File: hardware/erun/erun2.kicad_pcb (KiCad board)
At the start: 2 copper layers, 73.4 x 92.1 mm, 34 parts, among them J1 Conn_Coaxial, J10 Conn_01x03_Female, J2 HEIDENHAIN_MT25_TTL, J3 TRIGGER_TTL, J4 Conn_01x02_Female, J5 Conn_01x02_Female, J6 Conn_01x02_Female, J7 Conn_01x02_Female, J8 Conn_01x02_Female, J9 Conn_01x03_Female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

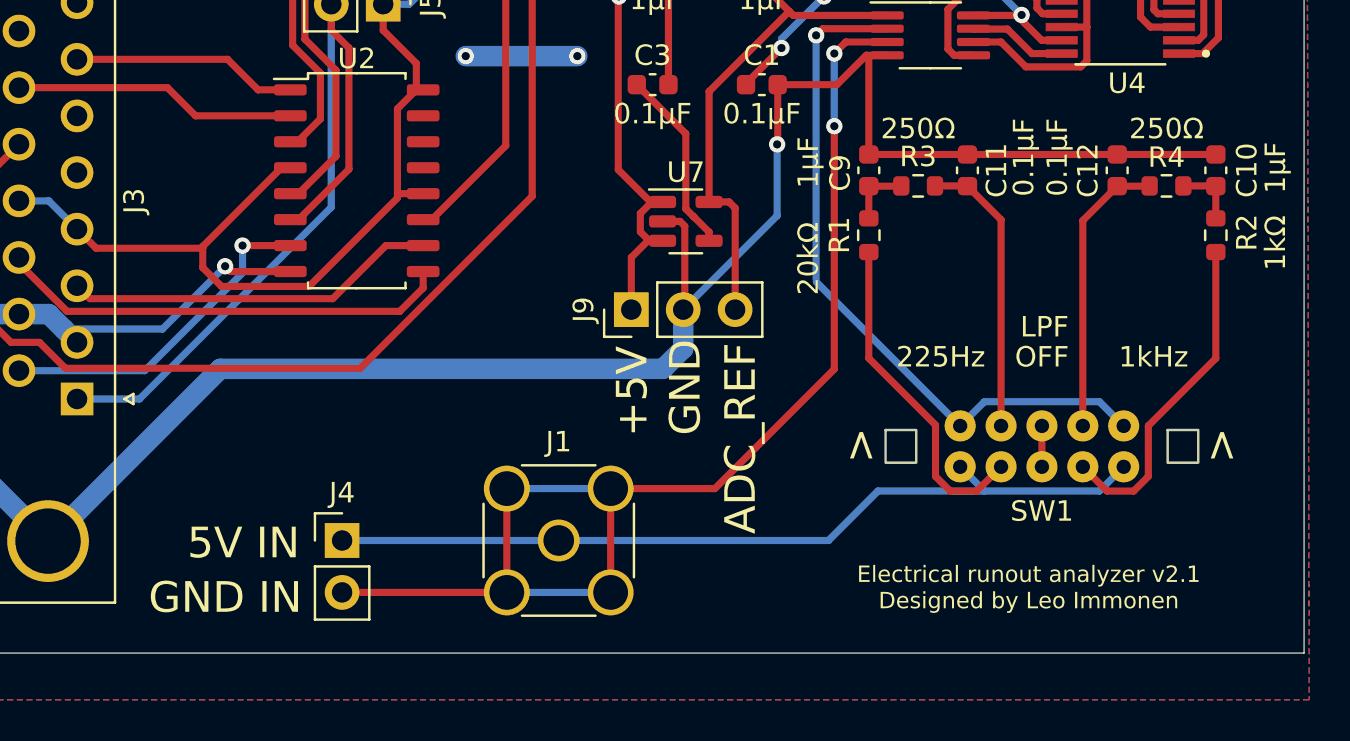
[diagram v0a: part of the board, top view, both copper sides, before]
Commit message: Added voltage divider
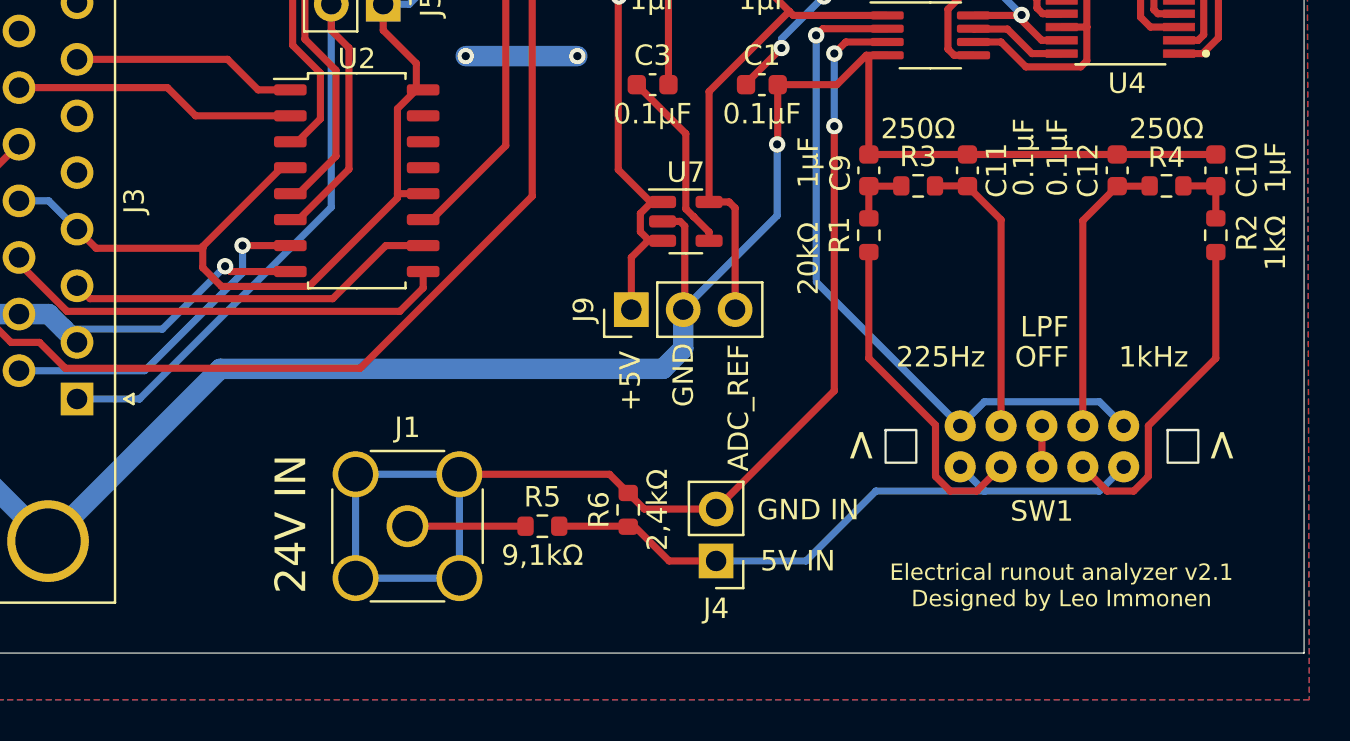
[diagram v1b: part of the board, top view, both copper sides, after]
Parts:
- added R5: 9,1kΩ, Resistor_SMD:R_0603_1608Metric, F.Cu at (48.2, 95.9)
- added R6: 2,4kΩ, Resistor_SMD:R_0603_1608Metric, F.Cu at (52.4, 95.1)
- moved J4 18.3 mm to (56.7, 97.6), turned to 180 degrees
- moved J1 7.43 mm to (41.6, 95.9)
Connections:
- J1 pad 1: /ANALOG_5V -> /ANALOG_24V
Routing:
- net /ANALOG_5V: track 41.4 -> 31.6 mm
- net /ANALOG_24V: track 0.00 -> 5.77 mm
- net /ANALOG_GND: track 60.0 -> 61.1 mm
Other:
- board text added: "24V IN"

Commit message: First version of PCB board v3.0
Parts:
- added JP1: SolderJumper_3_Open, Jumper:SolderJumper-3_P1.3mm_Open_Pad1.0x1.5mm_NumberLabels, F.Cu at (183.5, 104.0)
- added REF**: MODULE_RASPBERRY_PI_3_MODEL_B+, Raspberry-Pi-3:MODULE_RASPBERRY_PI_3_MODEL_B+, F.Cu at (132.8, 83.2)
- moved J3 190.2 mm to (215.2, 102.2), turned to 90 degrees
- moved J2 189.9 mm to (215.2, 36.9), turned to 90 degrees
- moved R5 150.1 mm to (194.2, 130.6)
- moved J1 149.7 mm to (187.6, 128.6)
- moved J10 148.9 mm to (207.1, 45.9)
- moved J4 145.8 mm to (198.9, 129.7)
- moved R6 145.2 mm to (194.2, 126.2), turned to 0 degrees
- moved C8 144.5 mm to (189.7, 71.3), turned to -90 degrees
- moved J6 143.6 mm to (183.3, 36.4)
- moved U2 139.7 mm to (178.8, 82.1), turned to 180 degrees
- moved C2 138.6 mm to (187.1, 106.3), turned to -90 degrees
- moved J5 137.8 mm to (176.3, 93.2), turned to 0 degrees
- moved U3 136.3 mm to (173.8, 50.4)
- moved U6 135.8 mm to (202.4, 73.8)
- moved SW1 134.7 mm to (206.1, 110.5), turned to 90 degrees
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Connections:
- U7 pad 3: +5V -> Net-(U7-Pad3)
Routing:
- net GND: track 444.5 -> 163.5 mm, vias 13 -> 5
- net +5V: track 248.3 -> 409.4 mm, vias 5 -> 4
- net /S1_A0_HV-: track 10.4 -> 78.3 mm
- net /S1_A0_HV+: track 13.2 -> 72.9 mm
- net /S2_A0_HV-: track 11.1 -> 66.1 mm
- net /S2_A0_HV+: track 13.8 -> 63.7 mm
- net /S1_A1_HV-: track 16.2 -> 59.7 mm
- net /S2_A2_HV-: track 22.3 -> 65.1 mm
- net /S2_A1_HV-: track 16.6 -> 59.4 mm, vias 1 -> 0
- net /S2_A2_HV+: track 18.3 -> 60.4 mm
- net /S1_A1_HV+: track 29.2 -> 62.3 mm, vias 0 -> 1
- net /S2_A1_LV: track 41.3 -> 8.63 mm, vias 1 -> 0
- net /S2_A2_LV: track 41.9 -> 9.23 mm
- net /S1_A2_LV: track 41.5 -> 8.88 mm, vias 1 -> 0
- net +3V3: track 148.5 -> 119.1 mm, vias 2 -> 3
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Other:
- board size 73.4 x 92.1 mm -> 121.3 x 120.9 mm
- board text added: "Electrical runout analyzer v3.0 Designed by Leo Immonen"
- board text removed: ">"
- board text removed: "Electrical runout analyzer v2.1 Designed by Leo Immonen"

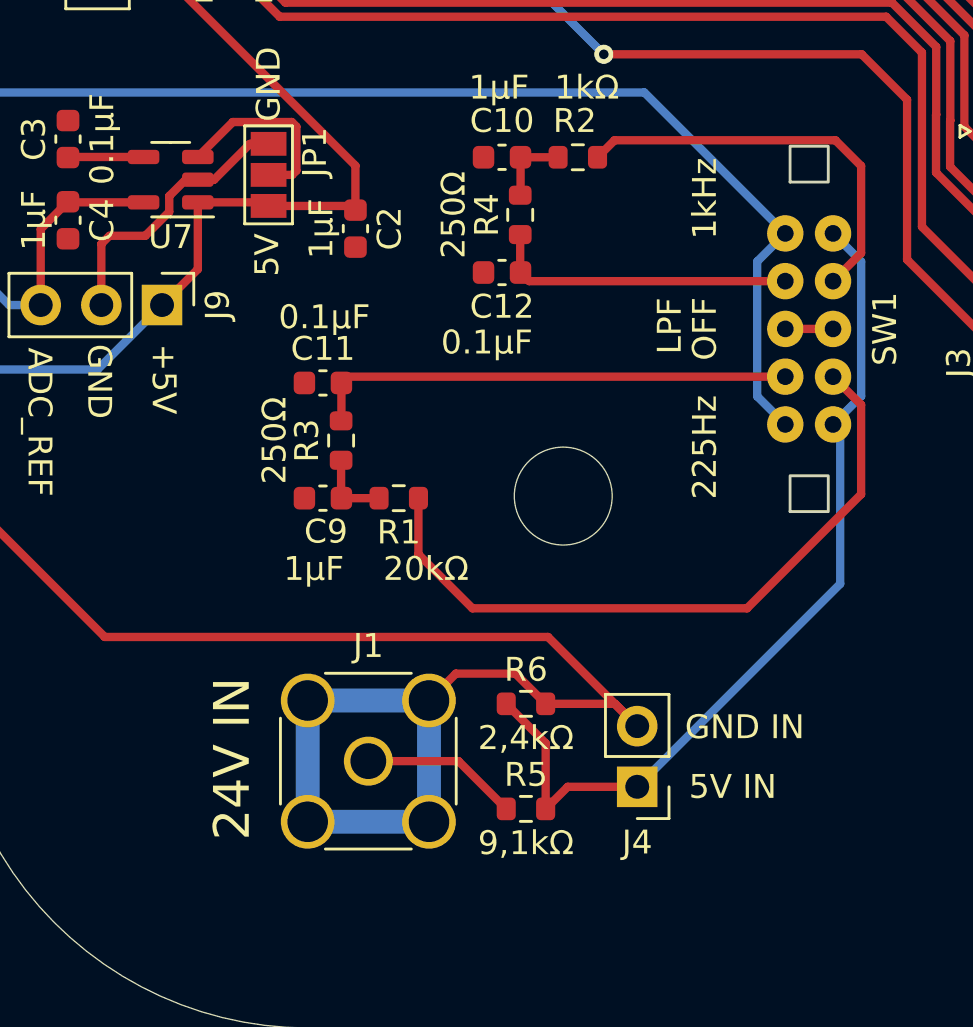
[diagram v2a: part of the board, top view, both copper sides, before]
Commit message: Changed SW1 hole shape and added analog text
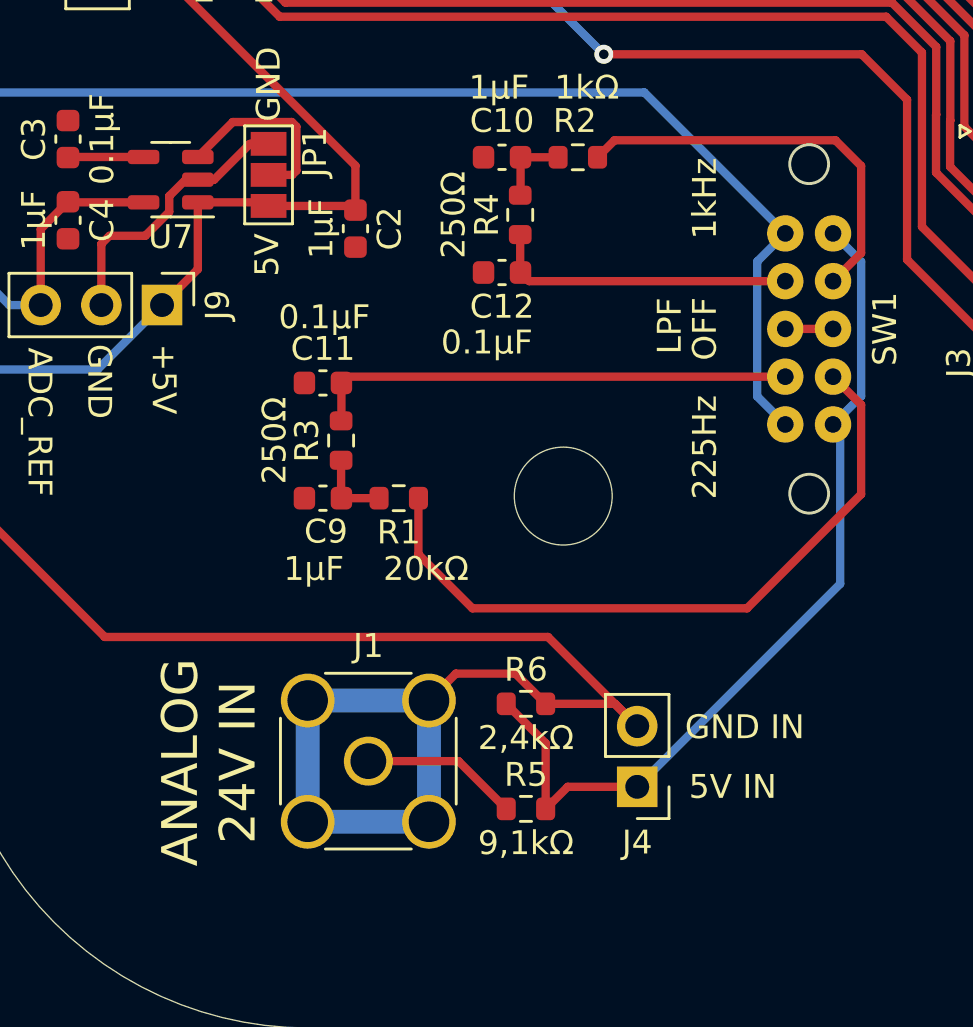
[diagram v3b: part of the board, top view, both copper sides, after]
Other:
- board text added: "ANALOG 24V IN"
- board text removed: "24V IN"
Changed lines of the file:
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@@
       (effects (font (size 1 1) (thickness 0.15)))
     )
-    (fp_rect (start 6.15 -0.8) (end 7.65 0.8) (layer "Edge.Cuts") (width 0.12) (fill none))
-    (fp_rect (start -7.65 -0.8) (end -6.15 0.8) (layer "Edge.Cuts") (width 0.12) (fill none))
+    (fp_circle (center -6.9 0) (end -6.086059 0) (layer "Edge.Cuts") (width 0.12) (fill none))
+    (fp_circle (center 6.9 0) (end 7.713941 0) (layer "Edge.Cuts") (width 0.12) (fill none))
     (fp_rect (start -7.25 -3.5) (end 7.25 3.5) (layer "F.CrtYd") (width 0.12) (fill none))
     (pad "1" thru_hole circle (at -2 1 90) (size 1.524 1.524) (drill 0.7) (layers *.Cu *.Mask)
@@
     (effects (font (size 1 1) (thickness 0.25)))
   )
-  (gr_text "24V IN" (at 181.94 128.5 90) (layer "F.SilkS")
+  (gr_text "ANALOG\n24V IN" (at 180.975 128.651 90) (layer "F.SilkS")
     (effects (font (size 1.5 1.5) (thickness 0.3)))
   )

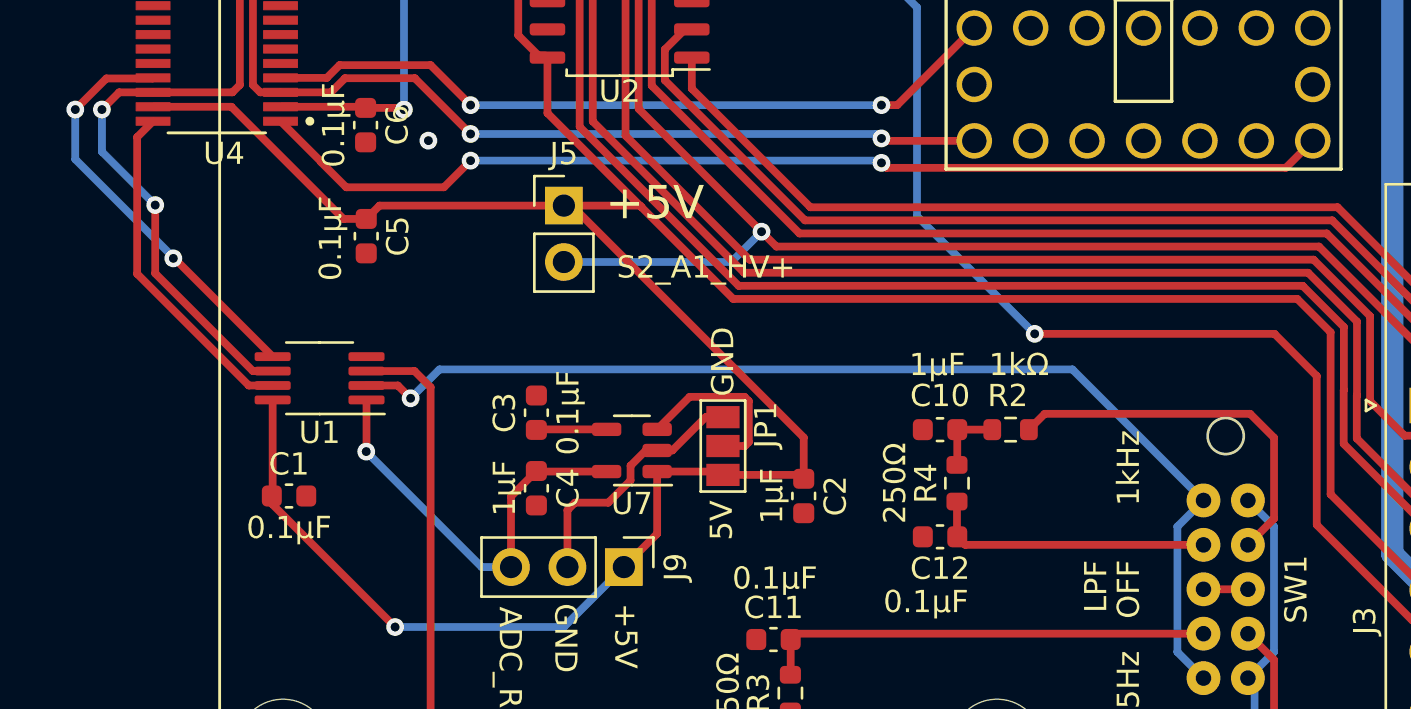
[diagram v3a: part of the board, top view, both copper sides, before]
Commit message: Fixed trace overlapping with hole and changed MCP3301 package from MSOP to SOIC
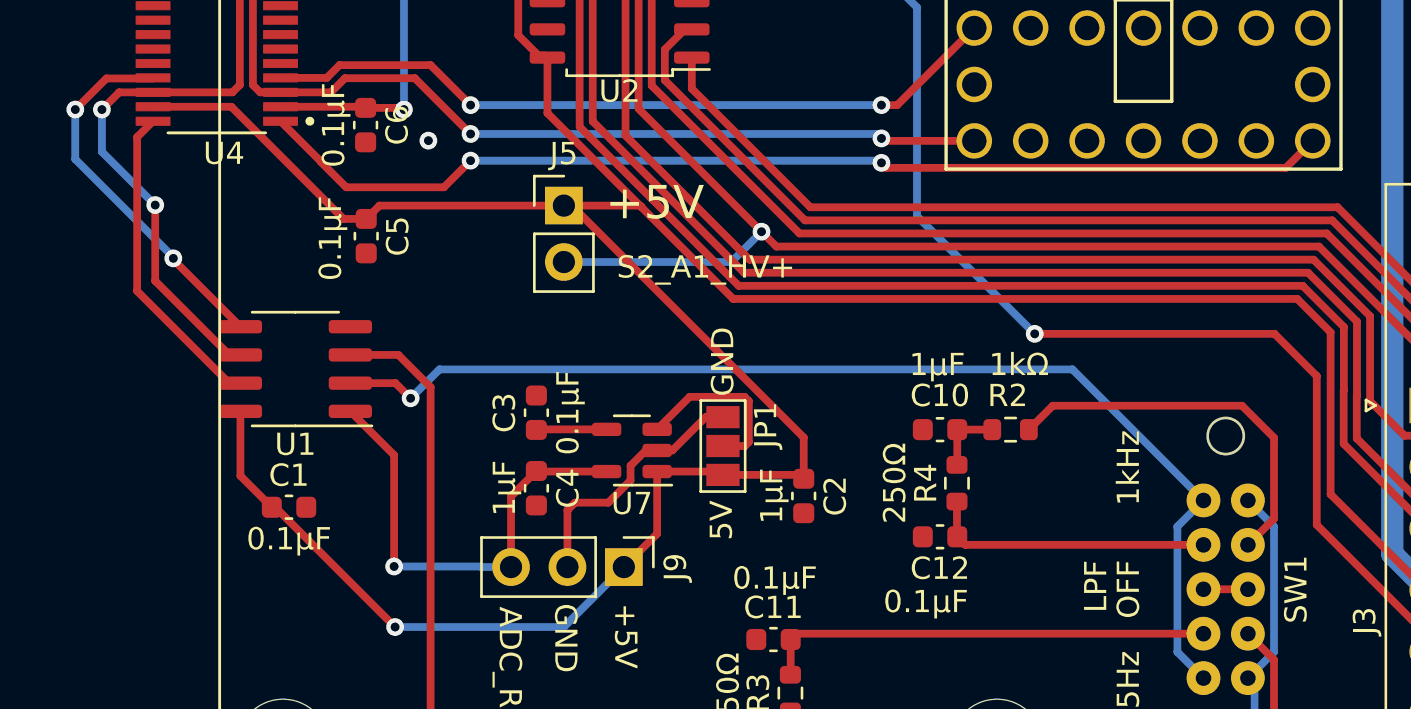
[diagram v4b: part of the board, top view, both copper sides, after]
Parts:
- U1: footprint Package_SO:MSOP-8_3x3mm_P0.65mm -> Package_SO:SOIC-8_3.9x4.9mm_P1.27mm
- moved U1 1.17 mm to (164.2, 100.6)
- moved C1 0.51 mm to (163.9, 106.8)
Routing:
- net /ADC_REF: track 19.0 -> 21.0 mm
- net /ADC_CS_HV: track 18.9 -> 17.0 mm
- net /ADC_MISO_HV: track 41.7 -> 40.2 mm
- net /ADC_CLK_HV: track 15.4 -> 14.3 mm
- net /ANALOG_GND: track 82.1 -> 83.1 mm
